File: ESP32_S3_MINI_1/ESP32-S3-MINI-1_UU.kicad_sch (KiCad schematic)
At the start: 53 parts, among them IC1 TPS6282533DMQR, IC2 BQ25185DLHR, J1 JST_2mm_LiPo, J2 USB4120-03-C, J3 Qwiic_Vertical, J4 Castellated_1x01, J5 Castellated_1x17, J6 Castellated_1x19, U2 ESP32-S3-MINI-1, U3 MAX17048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

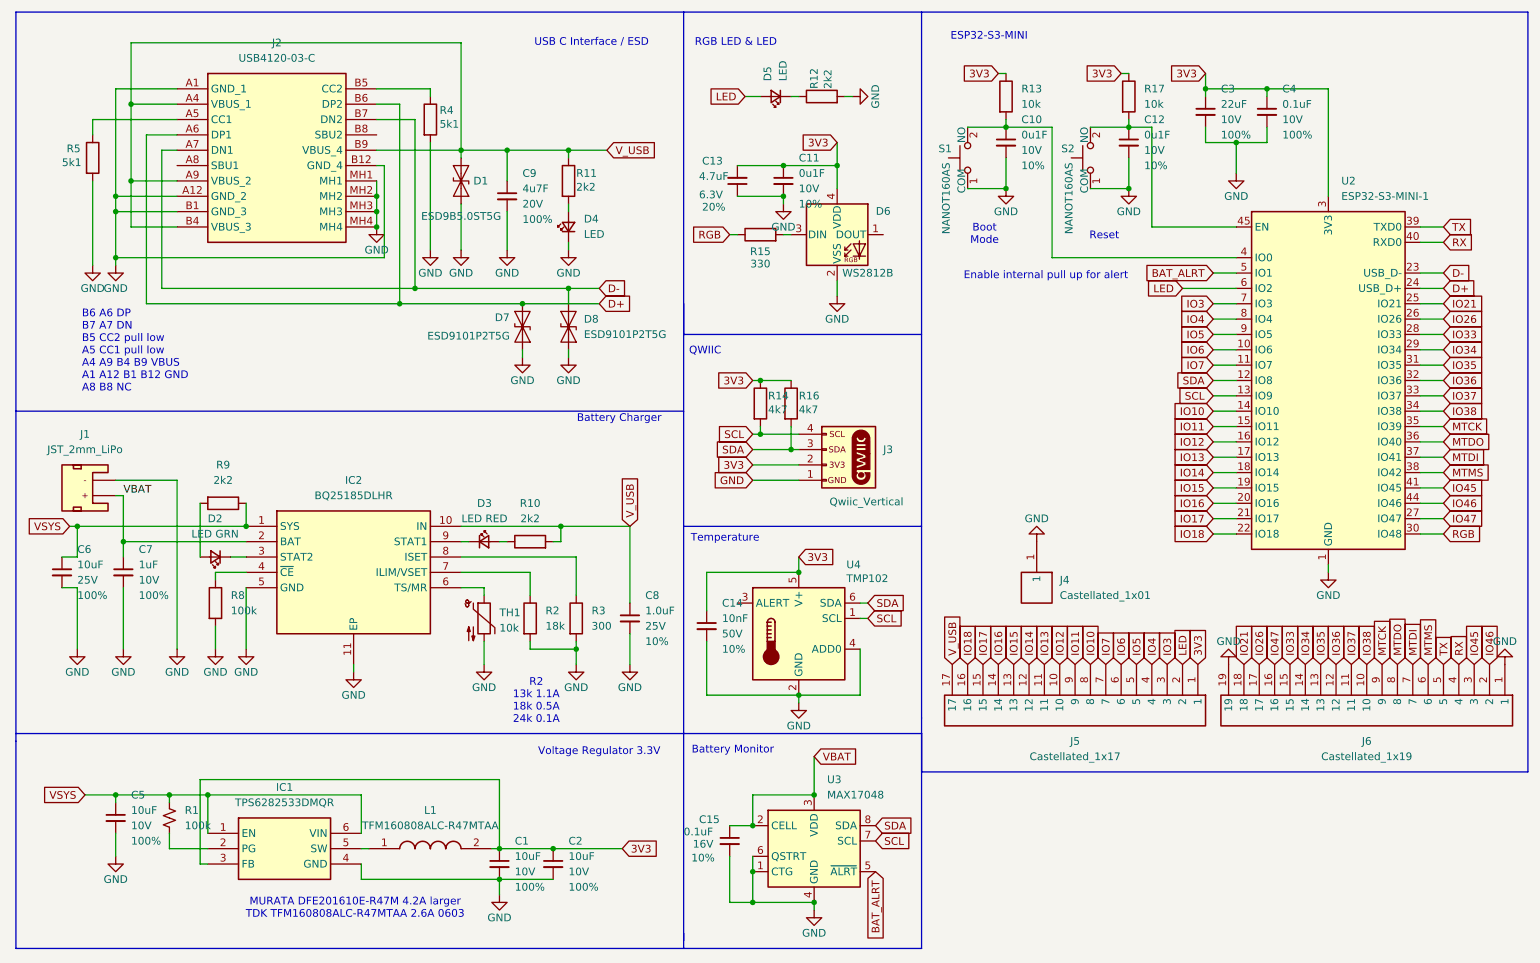
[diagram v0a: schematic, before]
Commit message: ESP32-S3-1 updates from 1U design
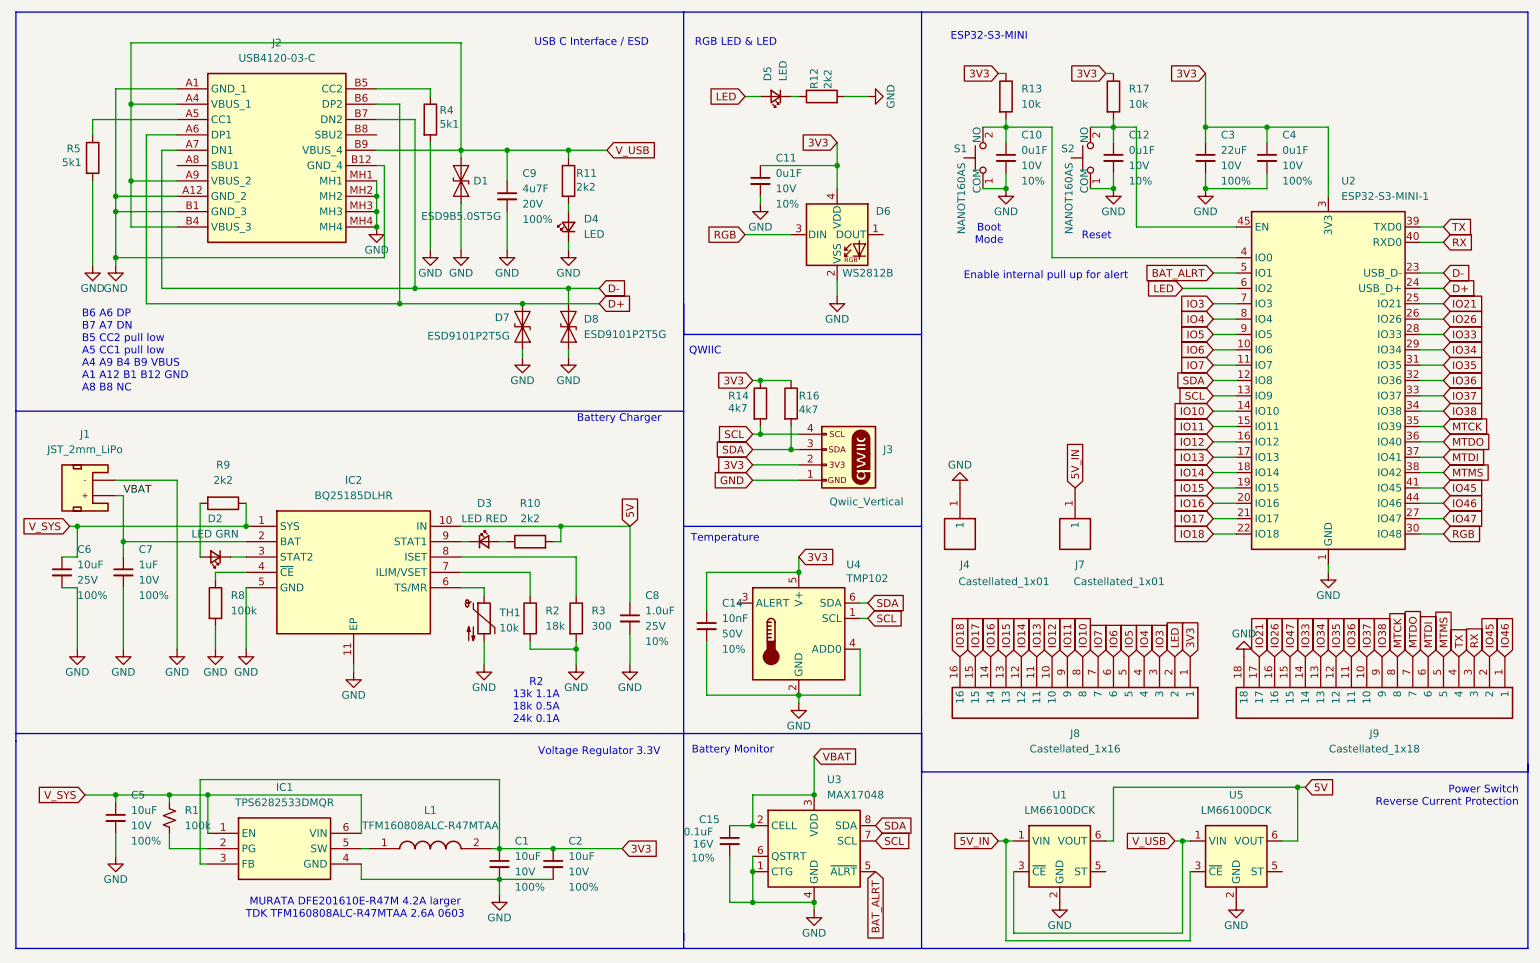
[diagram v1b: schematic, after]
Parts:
- removed C13: 4.7uF, PCM_SparkFun-Capacitor:C_0402_1005Metric, symbol PCM_SparkFun-Capacitor:4.7uF_0402_6.3V_10%
- removed J5: Castellated_1x17, ESP32:Castellated_1x017_P2.54mm_D0.80mm, symbol Castellated_Connectors:Castellated_1x17
- removed J6: Castellated_1x19, ESP32:Castellated_1x019_P2.54mm_D0.80mm, symbol Castellated_Connectors:Castellated_1x19
- removed R15: 330, PCM_SparkFun-Resistor:R_0402_1005Metric, symbol Device:R
- added J7: Castellated_1x01, ESP32:Castellated_1x01_P2.54mm_D0.80mm, symbol Castellated_Connectors:Castellated_1x01
- added J8: Castellated_1x16, Castellated_Connectors:Castellated_1x16_P2.54mm_D0.80mm, symbol Castellated_Connectors:Castellated_1x16
- added J9: Castellated_1x18, Castellated_Connectors:Castellated_1x18_P2.54mm_D0.80mm, symbol Castellated_Connectors:Castellated_1x18
- added U1, U5: LM66100DCK, Package_TO_SOT_SMD:SOT-363_SC-70-6, symbol Power_Management:LM66100DCK
- C4: value 0.1uF -> 0u1F; footprint PCM_SparkFun-Capacitor:C_0402_1005Metric -> Capacitor_SMD:C_0402_1005Metric
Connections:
- net 3V3: now also J8.1
- net GND: now also J9.18, U1.2 (GND), U5.2 (GND)
- net IO10: now also J8.8
- net IO11: now also J8.9
- net IO12: now also J8.10
- net IO13: now also J8.11
- net IO14: now also J8.12
- net IO15: now also J8.13
- net IO16: now also J8.14
- net IO17: now also J8.15
- net IO18: now also J8.16
- net IO21: now also J9.17
- net IO26: now also J9.16
- net IO3: now also J8.3
- net IO33: now also J9.14
- net IO34: now also J9.13
- net IO35: now also J9.12
- net IO36: now also J9.11
- net IO37: now also J9.10
- net IO38: now also J9.9
- net IO4: now also J8.4
- net IO45: now also J9.2
- net IO46: now also J9.1
- net IO47: now also J9.15
- net IO5: now also J8.5
- net IO6: now also J8.6
- net IO7: now also J8.7
- net LED: now also J8.2
- net MTCK: now also J9.8
- net MTDI: now also J9.6
- net MTDO: now also J9.7
- net MTMS: now also J9.5
- net RGB: now also D6.3 (DIN)
- net RX: now also J9.3
- net TX: now also J9.4
- net V_USB: now also U1.3 (~{CE}), U5.1 (VIN); no longer C8.1, IC2.10 (IN), R10.2
- net VSYS renamed V_SYS
- new net 5V: C8.1, IC2.10 (IN), R10.2, U1.6 (VOUT), U5.6 (VOUT)
- new net 5V_IN: J7.1, U1.1 (VIN), U5.3 (~{CE})
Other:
- note added: "Power Switch Reverse Current Protection"
- moved on the sheet: C10, C11, C12, C3, C4, J4, R17, S1

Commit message: Update ESP32 PCB projects and generated assets
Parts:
- removed TH1: 10k, PCM_SparkFun-Resistor:R_0402_1005Metric, symbol Device:Thermistor_NTC
- added TP3: TestPoint, ESP32-S3-MINI-1_Components:TestPoint_Pad_1.0x1.0mm, symbol Connector:TestPoint
- D7, D8: footprint Diode_SMD:D_SOD-923 -> ESP32-S3-MINI-1_Components:SODFL1006X40N; symbol Diode:ESD9B5.0ST5G -> ESP32-S3-MINI-1_Components:ESD9101P2T5G; Arrow Part Number (none) -> ESD9101P2T5G; Arrow Price/Stock (none) -> https://www.arrow.com/en/products/esd9101p2t5g/on-semicondu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; Height (none) -> 0.4; Manufacturer_Name (none) -> onsemi; Manufacturer_Part_Number (none) -> ESD9101P2T5G; Mouser Part Number (none) -> 863-ESD9101P2T5G; Mouser Price/Stock (none) -> https://www.mouser.co.uk/ProductDetail/onsemi/ESD9101P2T5G?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
- IC1: footprint TPS6282533DMQR -> ESP32-S3-MINI-1_Components:TPS6282533DMQR; symbol ESP32:TPS6282533DMQR -> ESP32-S3-MINI-1_Components:TPS6282533DMQR
- IC2: footprint ESP32:SON40P220X200X80-11N -> ESP32-S3-MINI-1_Components:SON40P220X200X80-11N
- J2: footprint ESP32:USB412003C -> ESP32-S3-MINI-1_Components:USB412003C
- J4, J7: footprint ESP32:Castellated_1x01_P2.54mm_D0.80mm -> Castellated_Connectors:Castellated_1x01_P2.54mm_D0.80mm
- L1: footprint ESP32:INDC1608X75N -> ESP32-S3-MINI-1_Components:INDC1608X75N; symbol ESP32:TFM160808ALC-R47MTAA -> ESP32-S3-MINI-1_Components:TFM160808ALC-R47MTAA
- S1, S2: footprint NANOT160AS -> ESP32-S3-MINI-1_Components:NANOT160AS
- U4: value TMP102 -> TMP112A; footprint PCM_SparkFun-Semiconductor-Standard:SOT-563 -> Package_TO_SOT_SMD:SOT-563; symbol PCM_SparkFun-Sensor:TMP102 -> ESP32-S3-MINI-1_Components:TMP112A
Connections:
- net D+: now also D7.1; no longer D7.2 (A2)
- net D-: now also D8.1; no longer D8.2 (A2)
- net GND: now also D1.2 (A2), D7.2, D8.2; no longer D1.1 (A1), D7.1 (A1), D8.1 (A1)
- net V_USB: now also D1.1 (A1); no longer D1.2 (A2)
- net at IC2.6 (TS/MR): now also TP3.1
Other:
- moved on the sheet: C14, D1
